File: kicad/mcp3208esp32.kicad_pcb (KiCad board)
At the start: 2 copper layers, 152.4 x 50.8 mm, 31 parts, among them J1 Conn_01x04, J2 Conn_01x04, J3 Conn_01x04, U1 LM324, U2 LM324

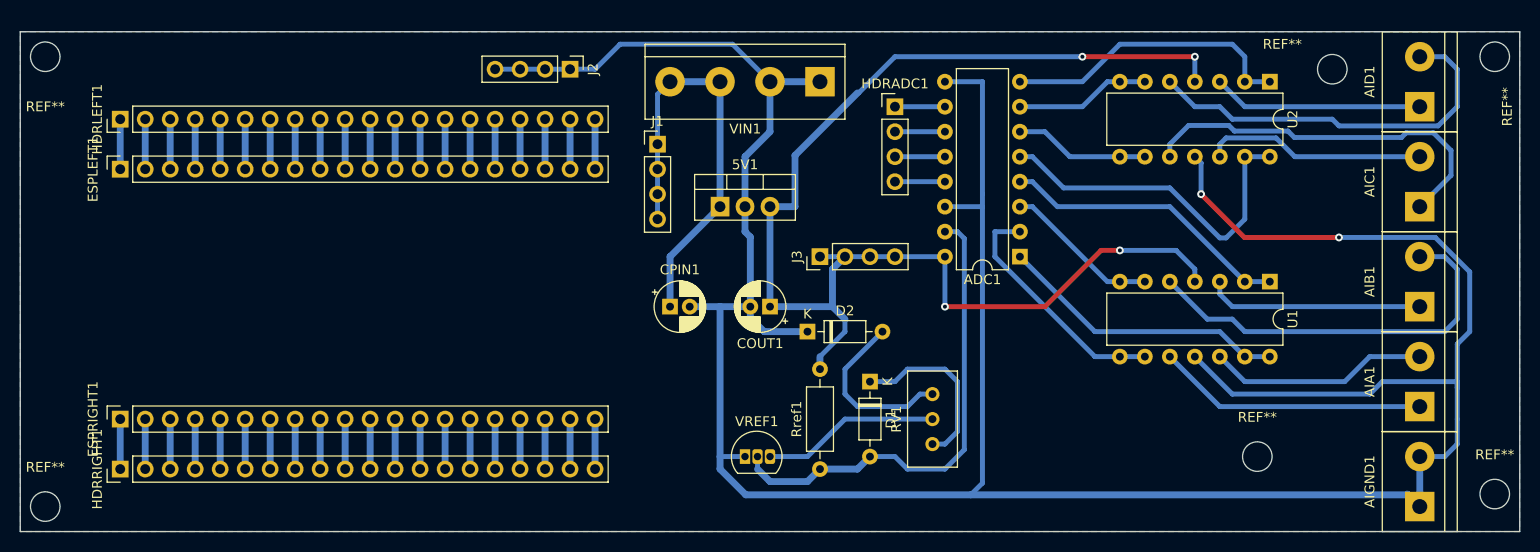
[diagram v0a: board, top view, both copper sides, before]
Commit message: Modified the source of the voltage reference
Now it uses the input voltage in contrast to before when the regulated 5V was the source for the reference voltage. This is an improvement because now the board can use 5V or 2.5V reference.
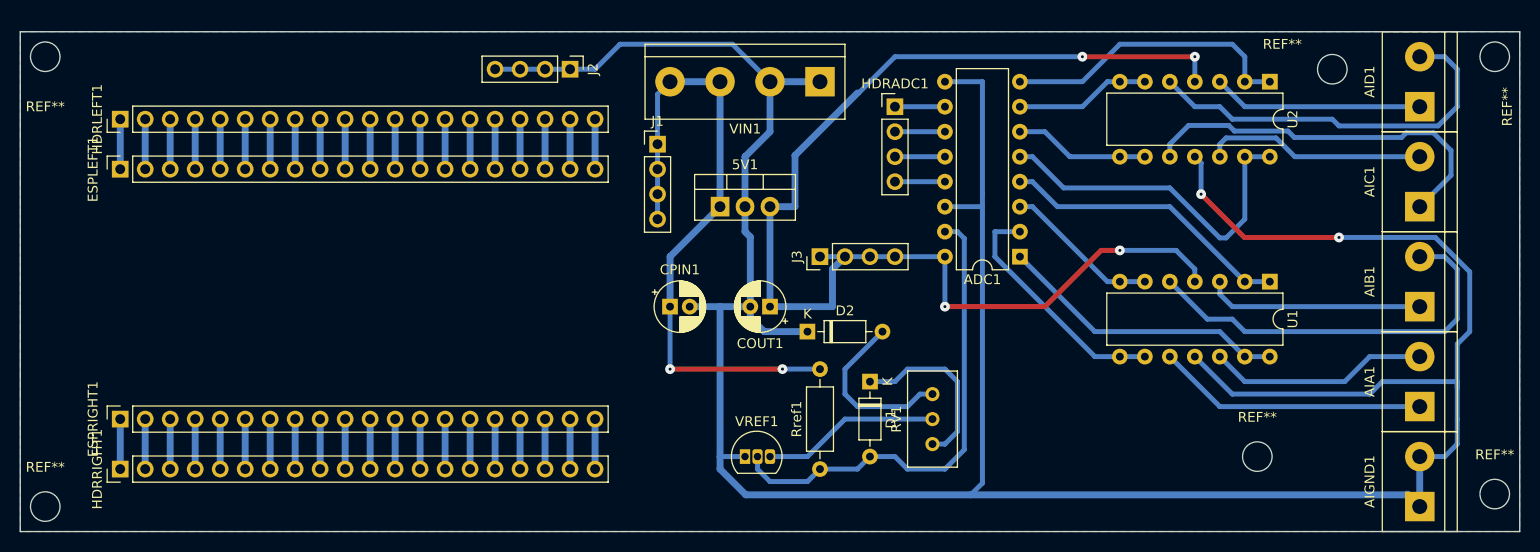
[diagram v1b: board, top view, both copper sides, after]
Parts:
- AIA1, AIB1, AIC1, AID1, AIGND1: value Conn_01x02_MountingPin -> Conn_01x02
- ESPLEFT1, ESPRIGHT1, HDRLEFT1, HDRRIGHT1: value Conn_01x20_MountingPin -> Conn_01x20
- VIN1: value Conn_01x04_MountingPin -> Conn_01x04
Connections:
- Rref1 pad 2: Net-(5V1-Pad3) -> Net-(5V1-Pad1)
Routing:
- net Net-(5V1-Pad1): track 44.5 -> 66.1 mm, vias 0 -> 2
- net Net-(5V1-Pad3): track 132.7 -> 124.8 mm

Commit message: Updated the pcb without the op amps
AGND and DGND are connected. Any signal conditioning will have to be done upstream.
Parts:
- removed the REF** at (209.6, 105.4)
- removed the REF** at (201.9, 144.8)
- removed the REF** at (226.1, 104.1)
- removed the REF** at (226.1, 148.6)
- removed the REF** at (78.7, 149.9)
- removed the REF** at (78.7, 104.1)
- removed U1, U2: LM324, Package_DIP:DIP-14_W7.62mm
- added JVREF1: Conn_01x04, Connector_PinHeader_2.54mm:PinHeader_1x04_P2.54mm_Vertical, F.Cu at (167.0, 123.2)
- added REF**: MountingHole_3mm, MountingHole:MountingHole_3mm, F.Cu at (80.0, 148.6)
- added REF**: MountingHole_3mm, MountingHole:MountingHole_3mm, F.Cu at (80.0, 105.4)
- added REF**: MountingHole_3mm, MountingHole:MountingHole_3mm, F.Cu at (224.8, 148.6)
- added REF**: MountingHole_3mm, MountingHole:MountingHole_3mm, F.Cu at (224.8, 105.4)
- moved AIA1 17.8 mm to (200.7, 139.7)
- moved AIB1 17.8 mm to (200.7, 129.5)
- moved AIC1 17.8 mm to (200.7, 119.4)
- moved AID1 17.8 mm to (200.7, 109.2)
- moved AIGND1 17.8 mm to (200.7, 149.9)
- moved JVOUT1 10.3 mm to (167.0, 128.3)
- moved 5V1 8.89 mm to (156.2, 119.4)
- moved HDRADC1 8.89 mm to (174.0, 109.2)
- moved JVIN1 8.89 mm to (149.9, 113.0)
- moved RV1 8.89 mm to (177.8, 138.4)
- moved Rref1 8.89 mm to (166.4, 146.1)
- moved VIN1 8.89 mm to (166.4, 106.7)
- moved ESPLEFT1 8.89 mm to (95.2, 115.6)
- moved ESPRIGHT1 8.89 mm to (95.2, 141.0)
- moved HDRLEFT1 8.89 mm to (95.2, 110.5)
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- renumbered J2 to JGND1, J1 to JVIN1, J3 to JVOUT1
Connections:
- AIA1 pad 1: Net-(AIA1-Pad1) -> Net-(ADC1-Pad1)
- AIA1 pad 2: Net-(AIA1-Pad2) -> Net-(ADC1-Pad2)
- AIB1 pad 1: Net-(AIB1-Pad1) -> Net-(ADC1-Pad3)
- AIB1 pad 2: Net-(AIB1-Pad2) -> Net-(ADC1-Pad4)
- AIC1 pad 1: Net-(AIC1-Pad1) -> Net-(ADC1-Pad5)
- AIC1 pad 2: Net-(AIC1-Pad2) -> Net-(ADC1-Pad6)
- AID1 pad 1: Net-(AID1-Pad1) -> Net-(ADC1-Pad7)
- AID1 pad 2: Net-(AID1-Pad2) -> Net-(ADC1-Pad8)
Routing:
- net Net-(5V1-Pad2): track 308.6 -> 196.5 mm, vias 2 -> 0
- net Net-(5V1-Pad3): track 124.8 -> 30.0 mm, vias 4 -> 0
- net Net-(AIB1-Pad2): track 41.3 -> 0.00 mm
- net Net-(AID1-Pad2): track 40.0 -> 0.00 mm
- net Net-(AIC1-Pad1): track 39.1 -> 0.00 mm
- net Net-(AIA1-Pad1): track 27.5 -> 0.00 mm
- net Net-(AIC1-Pad2): track 22.6 -> 0.00 mm
- net Net-(AIA1-Pad2): track 22.4 -> 0.00 mm
- net Net-(AIB1-Pad1): track 22.1 -> 0.00 mm
- net Net-(AID1-Pad1): track 21.4 -> 0.00 mm
- net Net-(ADC1-Pad5): track 36.0 -> 16.1 mm
- net Net-(ADC1-Pad8): track 30.0 -> 15.0 mm
- net Net-(ADC1-Pad15): track 48.9 -> 61.5 mm
- net Net-(ADC1-Pad4): track 29.6 -> 17.1 mm
- net Net-(ADC1-Pad1): track 29.6 -> 21.0 mm
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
